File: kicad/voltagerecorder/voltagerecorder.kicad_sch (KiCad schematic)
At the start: 38 parts

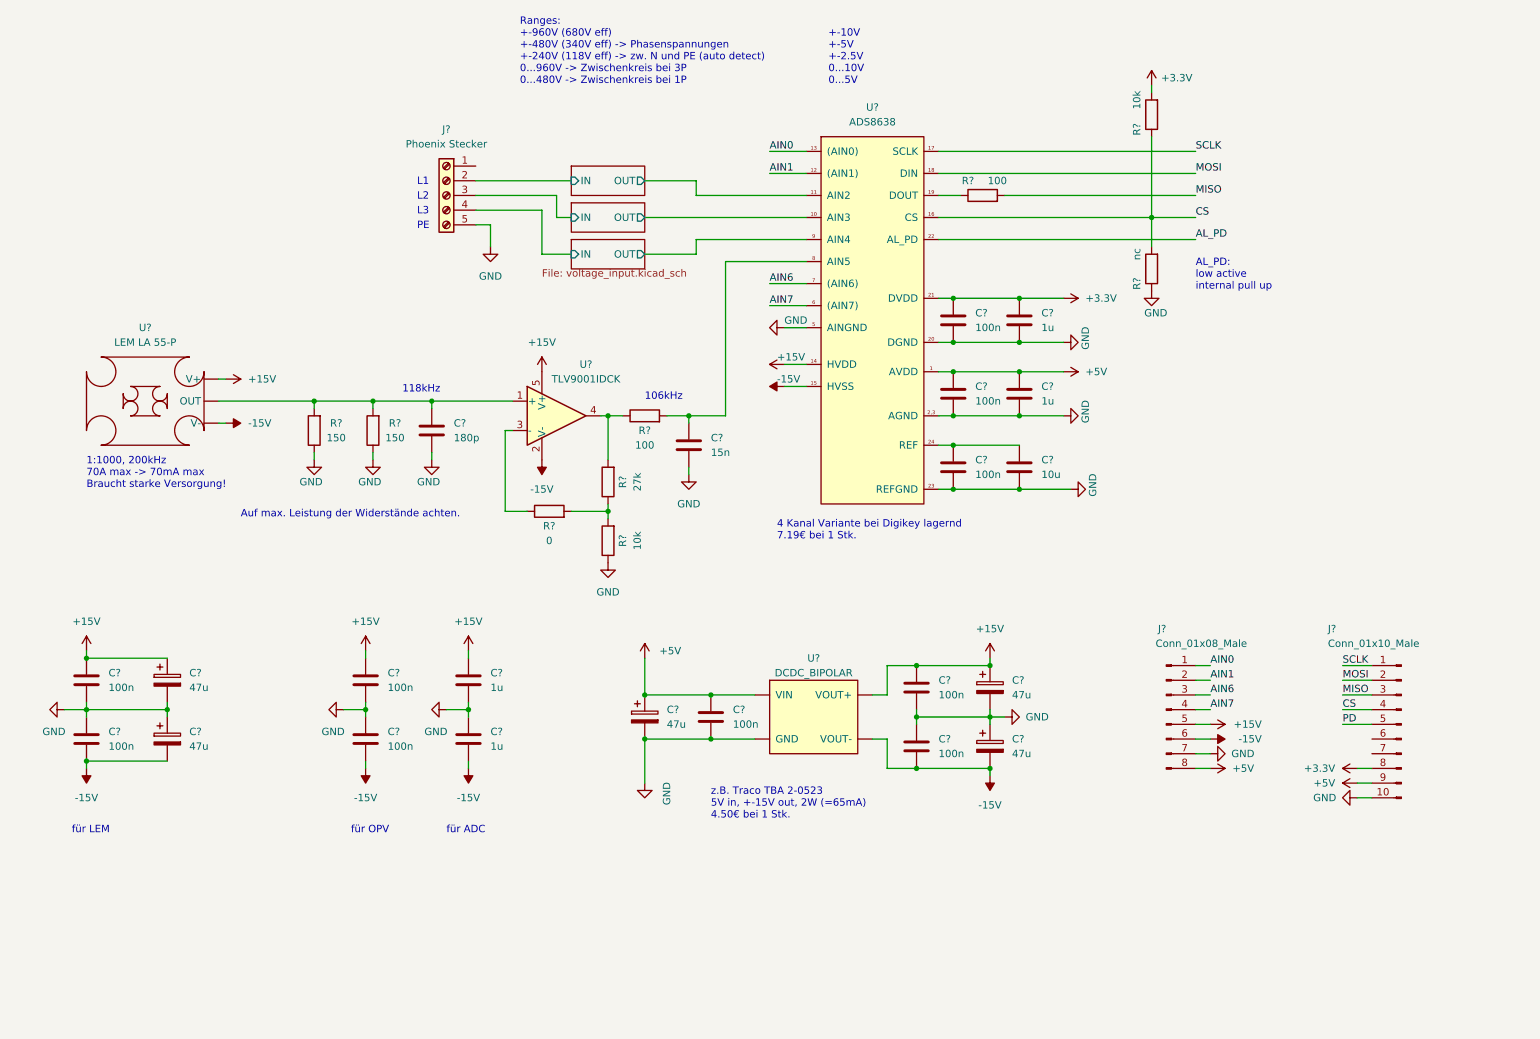
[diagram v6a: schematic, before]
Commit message: current_addon_single erstellt. Schaltplan aktualisiert.
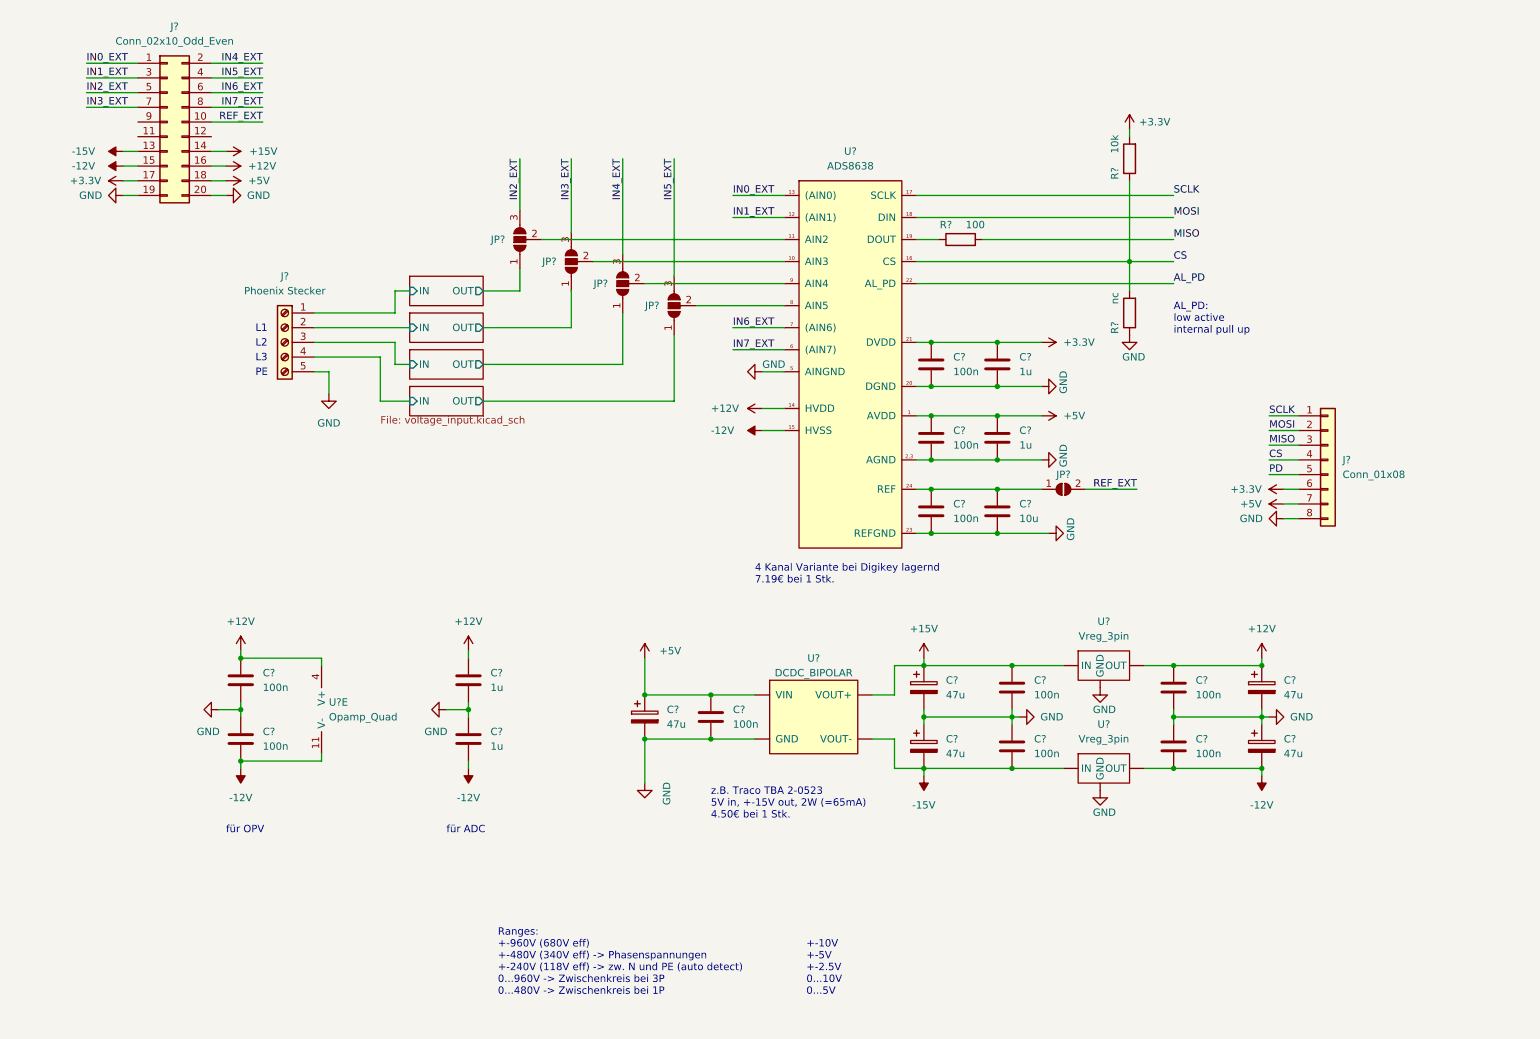
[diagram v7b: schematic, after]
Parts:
- removed C? (x2): 100n, symbol Device:C
- removed C?: 15n, symbol Device:C
- removed C? (x2): 47u, symbol Device:C_Polarized
- removed C?: 180p, symbol Device:C
- removed J?: Conn_01x10_Male, symbol Connector:Conn_01x10_Male
- removed J?: Conn_01x08_Male, symbol Connector:Conn_01x08_Male
- removed R?: 27k, symbol Device:R
- removed R?: 0, symbol Device:R
- removed R?: 100, symbol Device:R
- removed R? (x2): 150, symbol Device:R
- removed R?: 10k, symbol Device:R
- removed U?: LEM LA 55-P, symbol cf:CURRENTSENSOR
- removed U?: TLV9001IDCK, Package_TO_SOT_SMD:SOT-353_SC-70-5, symbol Amplifier_Operational:TLV9001IDCK
- added C? (x2): 100n, symbol Device:C
- added C? (x2): 47u, symbol Device:C_Polarized
- added J?: Conn_01x08, symbol Connector_Generic:Conn_01x08
- added J?: Conn_02x10_Odd_Even, symbol Connector_Generic:Conn_02x10_Odd_Even
- added JP?: SolderJumper_2_Open, symbol Jumper:SolderJumper_2_Open
- added JP? (x4): SolderJumper_3_Open, symbol Jumper:SolderJumper_3_Open
- added U? (x2): Vreg_3pin, symbol cf:Vreg_3pin
- added U?: Opamp_Quad, symbol Device:Opamp_Quad
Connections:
- net +15V: now also C?.1, J?.14 (Pin_14), U?. (OUT); no longer C?.1, C?.1, C?.1, U?.14 (HVDD)
- net +3.3V: now also J?.17 (Pin_17), J?.6 (Pin_6)
- net +5V: now also J?.18 (Pin_18), J?.7 (Pin_7)
- net -15V: now also C?.2, J?.13 (Pin_13), U?. (OUT); no longer C?.2, C?.2, C?.2, U?.15 (HVSS)
- net CS: now also J?.4 (Pin_4)
- net GND: now also C?.1, C?.2, C?.1, C?.1, C?.2, C?.2, J?.19 (Pin_19), J?.20 (Pin_20), J?.8 (Pin_8), U?. (OUT), U?. (OUT); no longer C?.1, C?.2
- net MISO: now also J?.3 (Pin_3)
- net MOSI: now also J?.2 (Pin_2)
- net PD: now also J?.5 (Pin_5)
- net SCLK: now also J?.1 (Pin_1)
- net voltage_input/OUT: now also JP?.1 (A); no longer U?.11 (AIN2)
- net voltage_input1/OUT: now also JP?.1 (A); no longer U?.10 (AIN3)
- net voltage_input2/OUT: now also JP?.1 (A); no longer U?.9 (AIN4)
- net at U?.8 (AIN5): now also JP?.2 (C)
- net at C?.1, C?.1, U?.24 (REF): now also JP?.1 (A)
- net voltage_input3/IN: now reaches J?.1 (Pin_1)
- net AIN0 renamed IN0_EXT
- net IN0_EXT: now also J?.1 (Pin_1)
- net AIN1 renamed IN1_EXT
- net IN1_EXT: now also J?.3 (Pin_3)
- net AIN6 renamed IN6_EXT
- net IN6_EXT: now also J?.6 (Pin_6)
- net AIN7 renamed IN7_EXT
- net IN7_EXT: now also J?.8 (Pin_8)
- new net: JP?.2 (C), U?.11 (AIN2)
- new net: JP?.2 (C), U?.10 (AIN3)
- new net: JP?.2 (C), U?.9 (AIN4)
- new net +12V: C?.1, C?.1, C?.1, C?.1, J?.16 (Pin_16), U?. (OUT), U?.14 (HVDD), U?.4 (V+)
- new net -12V: C?.2, C?.2, C?.2, C?.2, J?.15 (Pin_15), U?. (OUT), U?.11 (V-), U?.15 (HVSS)
- new net IN2_EXT: J?.5 (Pin_5), JP?.3 (B)
- new net IN3_EXT: J?.7 (Pin_7), JP?.3 (B)
- new net IN4_EXT: J?.2 (Pin_2), JP?.3 (B)
- new net IN5_EXT: J?.4 (Pin_4), JP?.3 (B)
- new net REF_EXT: J?.10 (Pin_10), JP?.2 (B)
- new net voltage_input3/OUT: JP?.1 (A)
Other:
- added sheet voltage_input3 (voltage_input.kicad_sch)
- note removed: "106kHz"
- note removed: "118kHz"
- note removed: "1:1000, 200kHz 70A max -> 70mA max Braucht starke Versorgung!"
- note removed: "Auf max. Leistung der Widerstände achten."
- note removed: "für LEM"
- moved on the sheet: C?, J?, R?, U?

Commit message: a
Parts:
- U1: renamed from U?; footprint (none) -> Package_SO:TSSOP-14_4.4x5mm_P0.65mm
- U3: renamed from U?; footprint (none) -> Package_DFN_QFN:QFN-24-1EP_4x4mm_P0.5mm_EP2.7x2.7mm
- U4: renamed from U?; footprint (none) -> Package_TO_SOT_SMD:SOT-89-3_Handsoldering
- gave numbers to parts that had none: 33
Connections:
- net +12V: now also U4.1 (OUT); no longer U4. (OUT)
- net +15V: now also U4.3 (IN); no longer U4. (OUT)
- net -12V: now also U5.1 (OUT); no longer U5. (OUT)
- net -15V: now also U5.3 (IN); no longer U5. (OUT)
- net GND: now also U4.2 (GND), U5.2 (GND); no longer U4. (OUT), U5. (OUT)
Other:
- moved on the sheet: C10, C11, C12, C13, C14, C9, J1, J2, J3, JP1, JP2, JP3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
